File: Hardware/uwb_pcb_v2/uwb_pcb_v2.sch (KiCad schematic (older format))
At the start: 13 parts, among them U1 TJA1051TK-3

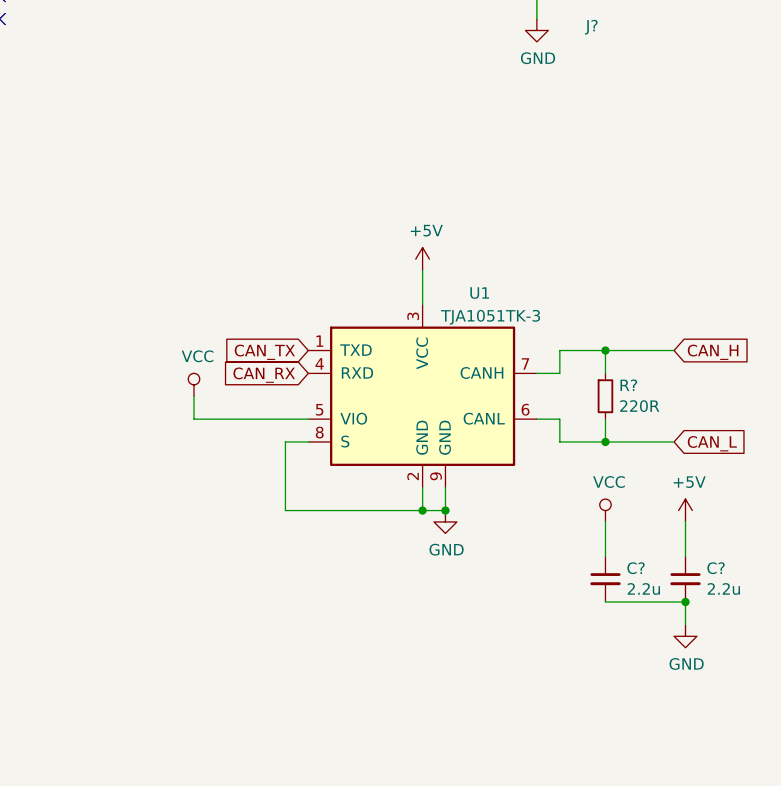
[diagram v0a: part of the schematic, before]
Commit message: added 3.3V can
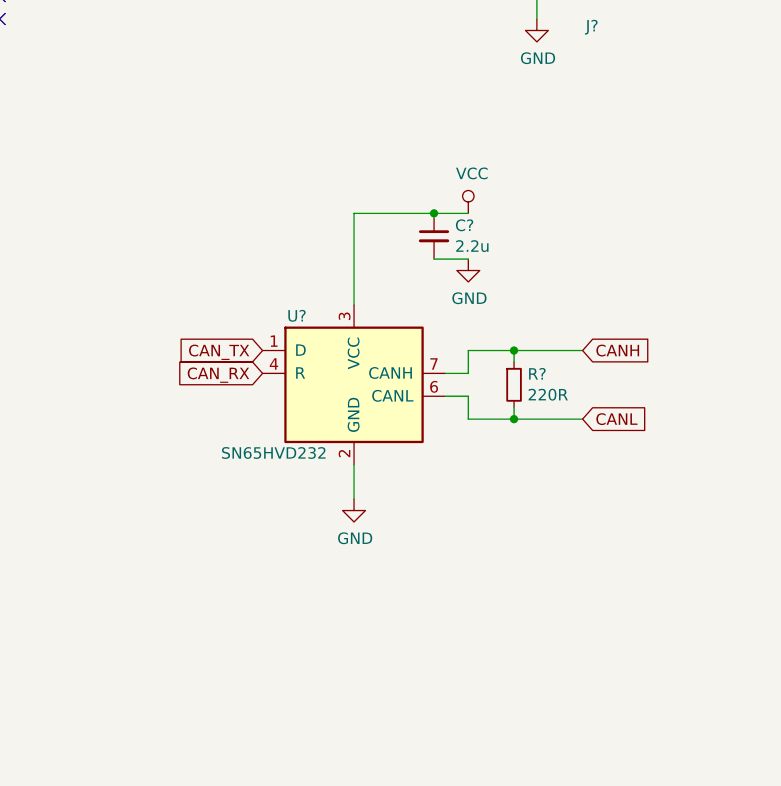
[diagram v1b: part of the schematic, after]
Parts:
- removed C?: 2.2u, symbol Device:C_Small
- removed R?: 220R, symbol Device:R_Small
- removed U1: TJA1051TK-3, Package_DFN_QFN:DFN-8-1EP_3x3mm_P0.65mm_EP1.55x2.4mm, symbol Interface_CAN_LIN:TJA1051TK-3
- added R?: 220R, symbol Device:R_Small
- added U?: SN65HVD232, Package_SO:SOIC-8_3.9x4.9mm_P1.27mm, symbol Interface_CAN_LIN:SN65HVD232
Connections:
- net CAN_RX: now also U?.4 (R)
- net CAN_TX: now also U?.1 (D)
- net GND: now also U?.2 (GND)
- net VCC: now also U?.3 (VCC)
- new net CANH: R?.1, U?.7 (CANH)
- new net CANL: R?.2, U?.6 (CANL)
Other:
- moved on the sheet: C?
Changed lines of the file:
@@
 	1    0    0    -1
 $EndComp
-$Comp
-L power:GND #PWR?
-U 1 1 5DCE2D5B
-P 8250 5700
-F 0 "#PWR?" H 8250 5450 50  0001 C CNN
-F 1 "GND" H 8255 5527 50  0000 C CNN
-F 2 "" H 8250 5700 50  0001 C CNN
-F 3 "" H 8250 5700 50  0001 C CNN
-	1    8250 5700
-	1    0    0    -1
-$EndComp
 Text GLabel 5900 5100 2    50   Input ~ 0
 CAN_TX
-Text GLabel 7650 5000 0    50   Input ~ 0
-CAN_TX
 Text GLabel 5900 5000 2    50   Input ~ 0
 CAN_RX
-Text GLabel 7650 5100 0    50   Input ~ 0
-CAN_RX
-$Comp
-L Interface_CAN_LIN:TJA1051TK-3 U1
-U 1 1 5AEAF5BD
-P 8150 5200
-F 0 "U1" H 8400 5650 50  0000 C CNN
-F 1 "TJA1051TK-3" H 8450 5550 50  0000 C CNN
-F 2 "Package_DFN_QFN:DFN-8-1EP_3x3mm_P0.65mm_EP1.55x2.4mm" H 8150 4700 50  0001 C CIN
-F 3 "http://www.nxp.com/documents/data_sheet/TJA1051.pdf" H 8150 5200 50  0001 C CNN
-	1    8150 5200
-	1    0    0    -1
-$EndComp
-Wire Wire Line
-	8150 5600 8150 5700
-Wire Wire Line
-	8150 5700 8250 5700
-Wire Wire Line
-	8250 5600 8250 5700
-Connection ~ 8250 5700
-Wire Wire Line
-	8150 5700 7550 5700
-Wire Wire Line
-	7550 5700 7550 5400
-Wire Wire Line
-	7550 5400 7650 5400
-Connection ~ 8150 5700
-$Comp
-L power:VCC #PWR?
-U 1 1 5DCEAA0F
-P 7150 5200
-F 0 "#PWR?" H 7150 5050 50  0001 C CNN
-F 1 "VCC" H 7167 5373 50  0000 C CNN
-F 2 "" H 7150 5200 50  0001 C CNN
-F 3 "" H 7150 5200 50  0001 C CNN
-	1    7150 5200
-	1    0    0    -1
-$EndComp
-Wire Wire Line
-	7650 5300 7150 5300
-Wire Wire Line
-	7150 5300 7150 5200
-$Comp
-L power:+5V #PWR?
-U 1 1 5DCEAE64
-P 8150 4650
-F 0 "#PWR?" H 8150 4500 50  0001 C CNN
-F 1 "+5V" H 8165 4823 50  0000 C CNN
-F 2 "" H 8150 4650 50  0001 C CNN
-F 3 "" H 8150 4650 50  0001 C CNN
-	1    8150 4650
-	1    0    0    -1
-$EndComp
-Wire Wire Line
-	8150 4800 8150 4650
-$Comp
-L Device:R_Small R?
-U 1 1 5DCEB7B9
-P 8950 5200
-F 0 "R?" H 9009 5246 50  0000 L CNN
-F 1 "220R" H 9009 5155 50  0000 L CNN
-F 2 "" H 8950 5200 50  0001 C CNN
-F 3 "~" H 8950 5200 50  0001 C CNN
-	1    8950 5200
-	1    0    0    -1
-$EndComp
-Wire Wire Line
-	8650 5100 8750 5100
-Wire Wire Line
-	8750 5100 8750 5000
-Wire Wire Line
-	8750 5000 8950 5000
-Wire Wire Line
-	8950 5000 8950 5100
-Wire Wire Line
-	8650 5300 8750 5300
-Wire Wire Line
-	8750 5300 8750 5400
-Wire Wire Line
-	8750 5400 8950 5400
-Wire Wire Line
-	8950 5400 8950 5300
-Text GLabel 9250 5000 2    50   Input ~ 0
-CAN_H
-Text GLabel 9250 5400 2    50   Input ~ 0
-CAN_L
-Wire Wire Line
-	8950 5000 9250 5000
-Connection ~ 8950 5000
-Wire Wire Line
-	8950 5400 9250 5400
-Connection ~ 8950 5400
 $Comp
 L Device:C_Small C?
 U 1 1 5DCEC403
-P 8950 6000
-F 0 "C?" H 9042 6046 50  0000 L CNN
-F 1 "2.2u" H 9042 5955 50  0000 L CNN
-F 2 "" H 8950 6000 50  0001 C CNN
-F 3 "~" H 8950 6000 50  0001 C CNN
-	1    8950 6000
-	1    0    0    -1
-$EndComp
-$Comp
-L Device:C_Small C?
-U 1 1 5DCEC968
-P 9300 6000
-F 0 "C?" H 9392 6046 50  0000 L CNN
-F 1 "2.2u" H 9392 5955 50  0000 L CNN
-F 2 "" H 9300 6000 50  0001 C CNN
-F 3 "~" H 9300 6000 50  0001 C CNN
-	1    9300 6000
-	1    0    0    -1
-$EndComp
-$Comp
-L power:+5V #PWR?
-U 1 1 5DCED52C
-P 9300 5750
-F 0 "#PWR?" H 9300 5600 50  0001 C CNN
-F 1 "+5V" H 9315 5923 50  0000 C CNN
-F 2 "" H 9300 5750 50  0001 C CNN
-F 3 "" H 9300 5750 50  0001 C CNN
-	1    9300 5750
+P 8200 4500
+F 0 "C?" H 8292 4546 50  0000 L CNN
+F 1 "2.2u" H 8292 4455 50  0000 L CNN
+F 2 "" H 8200 4500 50  0001 C CNN
+F 3 "~" H 8200 4500 50  0001 C CNN
+	1    8200 4500
 	1    0    0    -1
 $EndComp
@@
 L power:VCC #PWR?
 U 1 1 5DCED866
-P 8950 5750
-F 0 "#PWR?" H 8950 5600 50  0001 C CNN
-F 1 "VCC" H 8967 5923 50  0000 C CNN
-F 2 "" H 8950 5750 50  0001 C CNN
-F 3 "" H 8950 5750 50  0001 C CNN
-	1    8950 5750
+P 8350 4400
+F 0 "#PWR?" H 8350 4250 50  0001 C CNN
+F 1 "VCC" H 8367 4573 50  0000 C CNN
+F 2 "" H 8350 4400 50  0001 C CNN
+F 3 "" H 8350 4400 50  0001 C CNN
+	1    8350 4400
 	1    0    0    -1
 $EndComp
 Wire Wire Line
-	8950 5750 8950 5900
-Wire Wire Line
-	9300 5750 9300 5900
+	8350 4400 8200 4400
 $Comp
 L power:GND #PWR?
 U 1 1 5DCEDA1E
-P 9300 6200
-F 0 "#PWR?" H 9300 5950 50  0001 C CNN
-F 1 "GND" H 9305 6027 50  0000 C CNN
-F 2 "" H 9300 6200 50  0001 C CNN
-F 3 "" H 9300 6200 50  0001 C CNN
-	1    9300 6200
+P 8350 4600
+F 0 "#PWR?" H 8350 4350 50  0001 C CNN
+F 1 "GND" H 8355 4427 50  0000 C CNN
+F 2 "" H 8350 4600 50  0001 C CNN
+F 3 "" H 8350 4600 50  0001 C CNN
+	1    8350 4600
 	1    0    0    -1
 $EndComp
-Wire Wire Line
-	9300 6200 9300 6100
-Wire Wire Line
-	9300 6100 8950 6100
-Connection ~ 9300 6100
 Text GLabel 4700 3150 0    50   Input ~ 0
 SPI_SO
@@
 	1    0    0    -1
 $EndComp
+$Comp
+L Interface_CAN_LIN:SN65HVD232 U?
+U 1 1 5DD3AEDD
+P 7850 5100
+F 0 "U?" H 7600 5350 50  0000 C CNN
+F 1 "SN65HVD232" H 7500 4750 50  0000 C CNN
+F 2 "Package_SO:SOIC-8_3.9x4.9mm_P1.27mm" H 7850 4600 50  0001 C CNN
+F 3 "http://www.ti.com/lit/ds/symlink/sn65hvd230.pdf" H 7750 5500 50  0001 C CNN
+	1    7850 5100
+	1    0    0    -1
+$EndComp
+Wire Wire Line
+	8350 4600 8200 4600
+Wire Wire Line
+	7850 4800 7850 4400
+Wire Wire Line
+	7850 4400 8200 4400
+Connection ~ 8200 4400
+Text GLabel 8850 5000 2    50   Input ~ 0
+CANH
+Text GLabel 8850 5300 2    50   Input ~ 0
+CANL
+$Comp
+L Device:R_Small R?
+U 1 1 5DD425DF
+P 8550 5150
+F 0 "R?" H 8609 5196 50  0000 L CNN
+F 1 "220R" H 8609 5105 50  0000 L CNN
+F 2 "" H 8550 5150 50  0001 C CNN
+F 3 "~" H 8550 5150 50  0001 C CNN
+	1    8550 5150
+	1    0    0    -1
+$EndComp
+Wire Wire Line
+	8250 5100 8350 5100
+Wire Wire Line
+	8350 5100 8350 5000
+Wire Wire Line
+	8350 5000 8550 5000
+Wire Wire Line
+	8250 5200 8350 5200
+Wire Wire Line
+	8350 5200 8350 5300
+Wire Wire Line
+	8350 5300 8550 5300
+Wire Wire Line
+	8550 5050 8550 5000
+Connection ~ 8550 5000
+Wire Wire Line
+	8550 5000 8850 5000
+Wire Wire Line
+	8550 5250 8550 5300
+Connection ~ 8550 5300
+Wire Wire Line
+	8550 5300 8850 5300
+$Comp
+L power:GND #PWR?
+U 1 1 5DD4323E
+P 7850 5650
+F 0 "#PWR?" H 7850 5400 50  0001 C CNN
+F 1 "GND" H 7855 5477 50  0000 C CNN
+F 2 "" H 7850 5650 50  0001 C CNN
+F 3 "" H 7850 5650 50  0001 C CNN
+	1    7850 5650
+	1    0    0    -1
+$EndComp
+Wire Wire Line
+	7850 5500 7850 5650
+Text GLabel 7450 5000 0    50   Input ~ 0
+CAN_TX
+Text GLabel 7450 5100 0    50   Input ~ 0
+CAN_RX
 $EndSCHEMATC

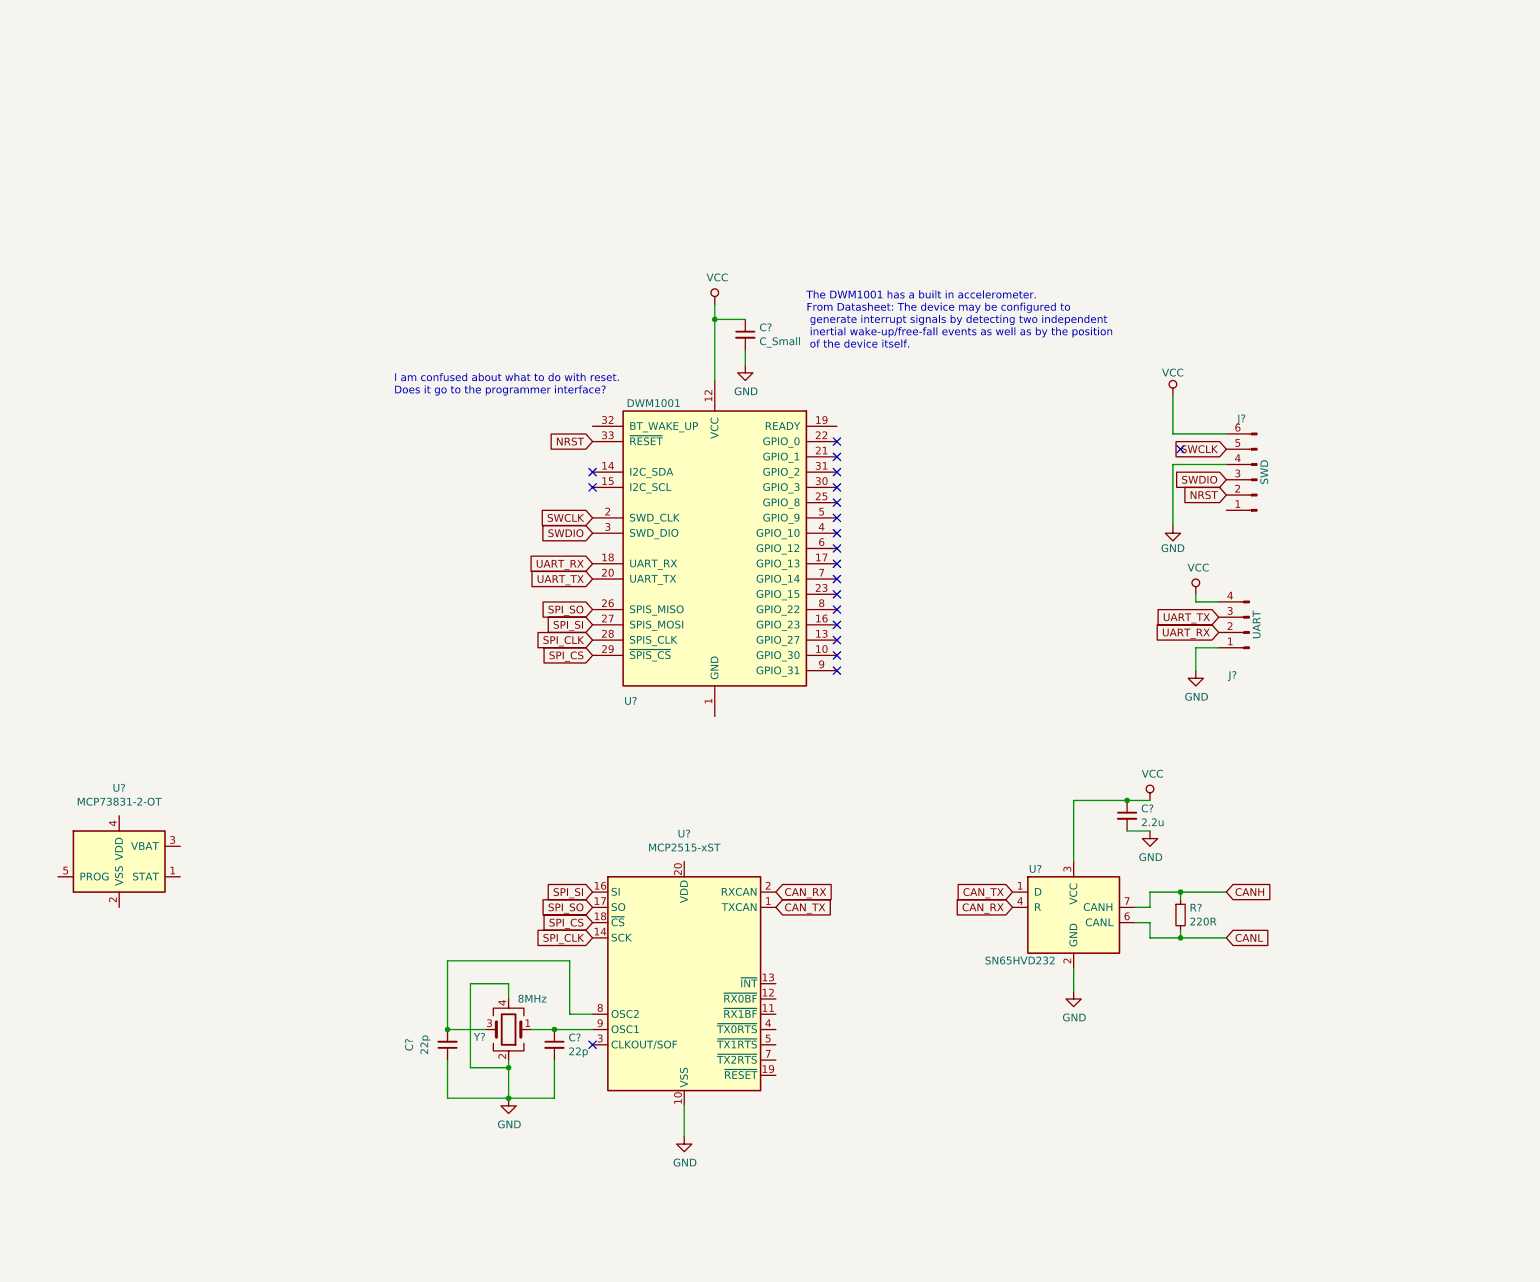
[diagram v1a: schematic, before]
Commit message: UWB V2: adding voltage regulator and some other tweaking-about
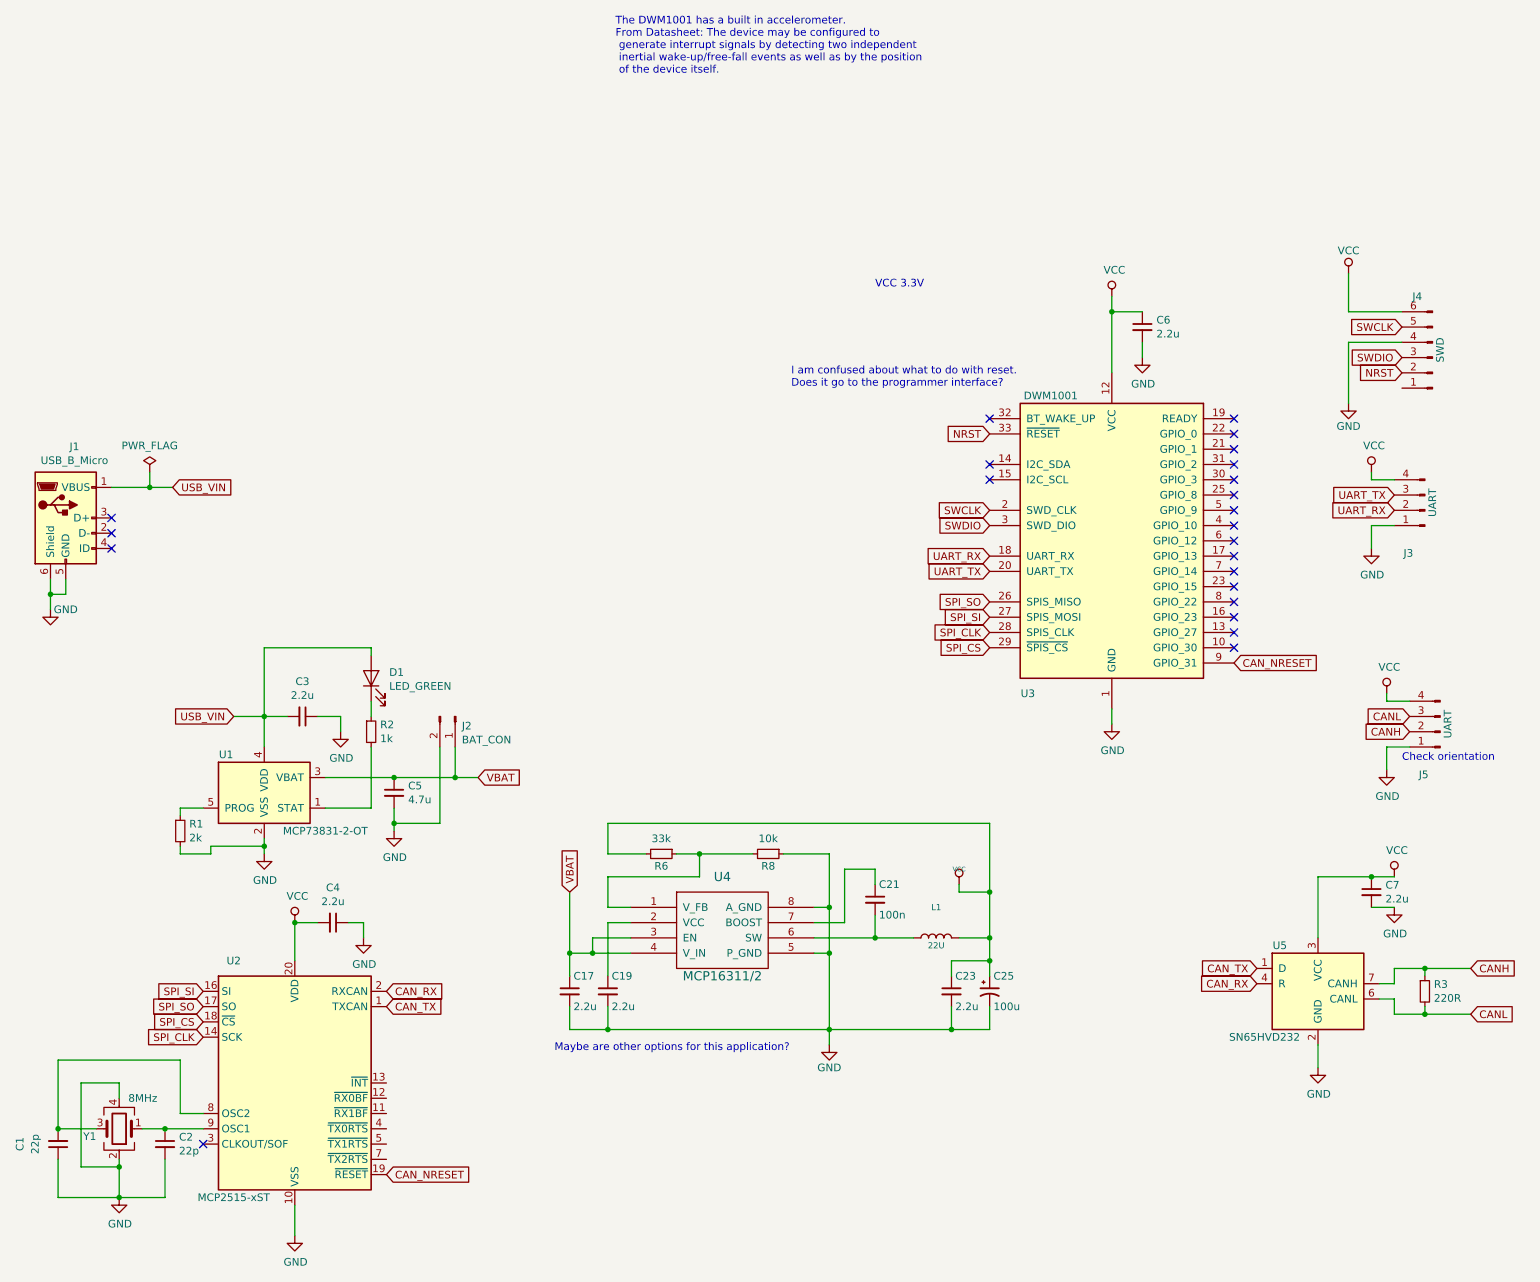
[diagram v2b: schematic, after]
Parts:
- added C17, C19, C23: 2.2u, Capacitor_SMD:C_0603_1608Metric, symbol Device:C_Small
- added C21: 100n, Capacitor_SMD:C_0603_1608Metric, symbol Device:C_Small
- added C25: 100u, Capacitor_Tantalum_SMD:CP_EIA-3528-12_Kemet-T, symbol Device:CP1_Small
- added C3, C4: 2.2u, symbol Device:C_Small
- added C5: 4.7u, symbol Device:C_Small
- added D1: LED_GREEN, symbol Device:LED
- added J1: USB_B_Micro, Connector_USB:USB_Micro-B_Molex-105017-0001, symbol Connector:USB_B_Micro
- added J2: BAT_CON, symbol Connector:Conn_01x02_Male
- added J5: UART, symbol Connector:Conn_01x04_Male
- added L1: 22U, Inductor_SMD:L_Taiyo-Yuden_MD-5050, symbol Device:L
- added R1: 2k, symbol Device:R_Small
- added R2: 1k, symbol Device:R_Small
- added R6: 33k, Resistor_SMD:R_0603_1608Metric, symbol Device:R_Small
- added R8: 10k, Resistor_SMD:R_0603_1608Metric, symbol Device:R_Small
- added U4: MCP16311/2, Package_SO:MSOP-8_3x3mm_P0.65mm, symbol crf_1:MCP16311_2
- C6: renamed from C?; value C_Small -> 2.2u
- U1: renamed from U?; OrderN (none) -> MCP73831T-2ATI/OTCT-ND
- U2: renamed from U?; OrderN (none) -> MCP2515T-I/STCT-ND
- gave numbers to parts that had none: 9
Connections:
- net CANH: now also J5.2 (Pin_2)
- net CANL: now also J5.3 (Pin_3)
- net GND: now also U1.2 (VSS), U3.1 (GND), U3.11 (GND), U3.24 (GND), U3.34 (GND), C17.2, C19.2, C23.2, C25.2, C3.1, C4.1, C5.2, J1.5 (GND), J1.6 (Shield), J2.2 (Pin_2), J5.1 (Pin_1), R1.2, R8.1, U4.5 (P_GND), U4.8 (A_GND)
- net VCC: now also U2.20 (VDD), C23.1, C25.1, C4.2, J5.4 (Pin_4), L1.2, R6.2
- net CAN_NRESET: now reaches U3.9 (GPIO_31)
- net CAN_NRESET: now also U2.19 (~RESET)
- net at U1.1 (STAT): now also R2.2
- net VBAT: now reaches U1.3 (VBAT)
- net VBAT: now also C17.1, C5.1, J2.1 (Pin_1), U4.3 (EN), U4.4 (V_IN)
- net USB_VIN: now reaches U1.4 (VDD)
- net USB_VIN: now also C3.2, D1.2 (A), J1.1 (VBUS)
- net at U1.5 (PROG): now also R1.1
- new net: R6.1, R8.2, U4.1 (V_FB)
- new net: C19.1, U4.2 (VCC)
- new net: C21.2, L1.1, U4.6 (SW)
- new net: C21.1, U4.7 (BOOST)
- new net: D1.1 (K), R2.1
- no-connect marks 20 -> 23
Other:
- note added: "Check orientation\n"
- note added: "Maybe are other options for this application?"
- note added: "VCC 3.3V\n"
- moved on the sheet: C1, C2, C6, C7, J3, J4, R3, U1, U2, U3, U5, Y1
